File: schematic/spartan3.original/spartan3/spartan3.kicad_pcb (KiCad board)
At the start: 2 copper layers, 215.9 x 160 mm, 242 parts, among them U1_clk_select_0 SPFT_Sliding_Switch-dynacore, U2 XC3S250E-4TQG144C

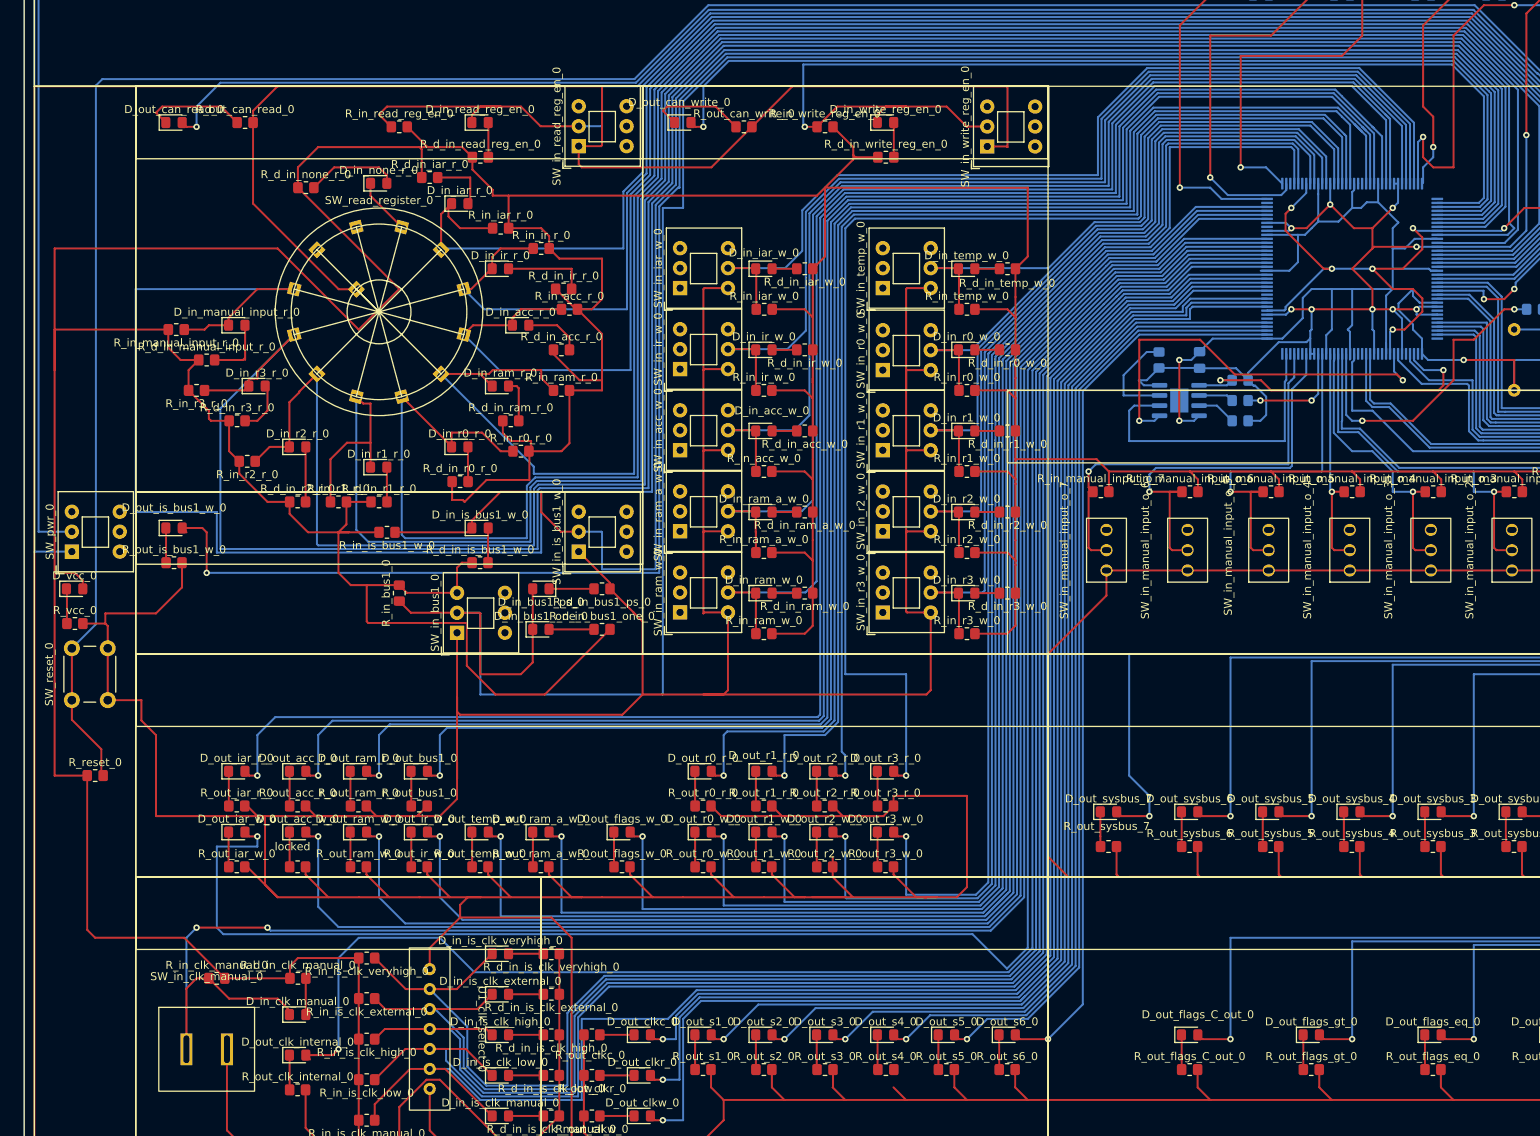
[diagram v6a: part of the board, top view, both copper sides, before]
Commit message: Tactile switch footprint updated. DRC rules checked/fixed
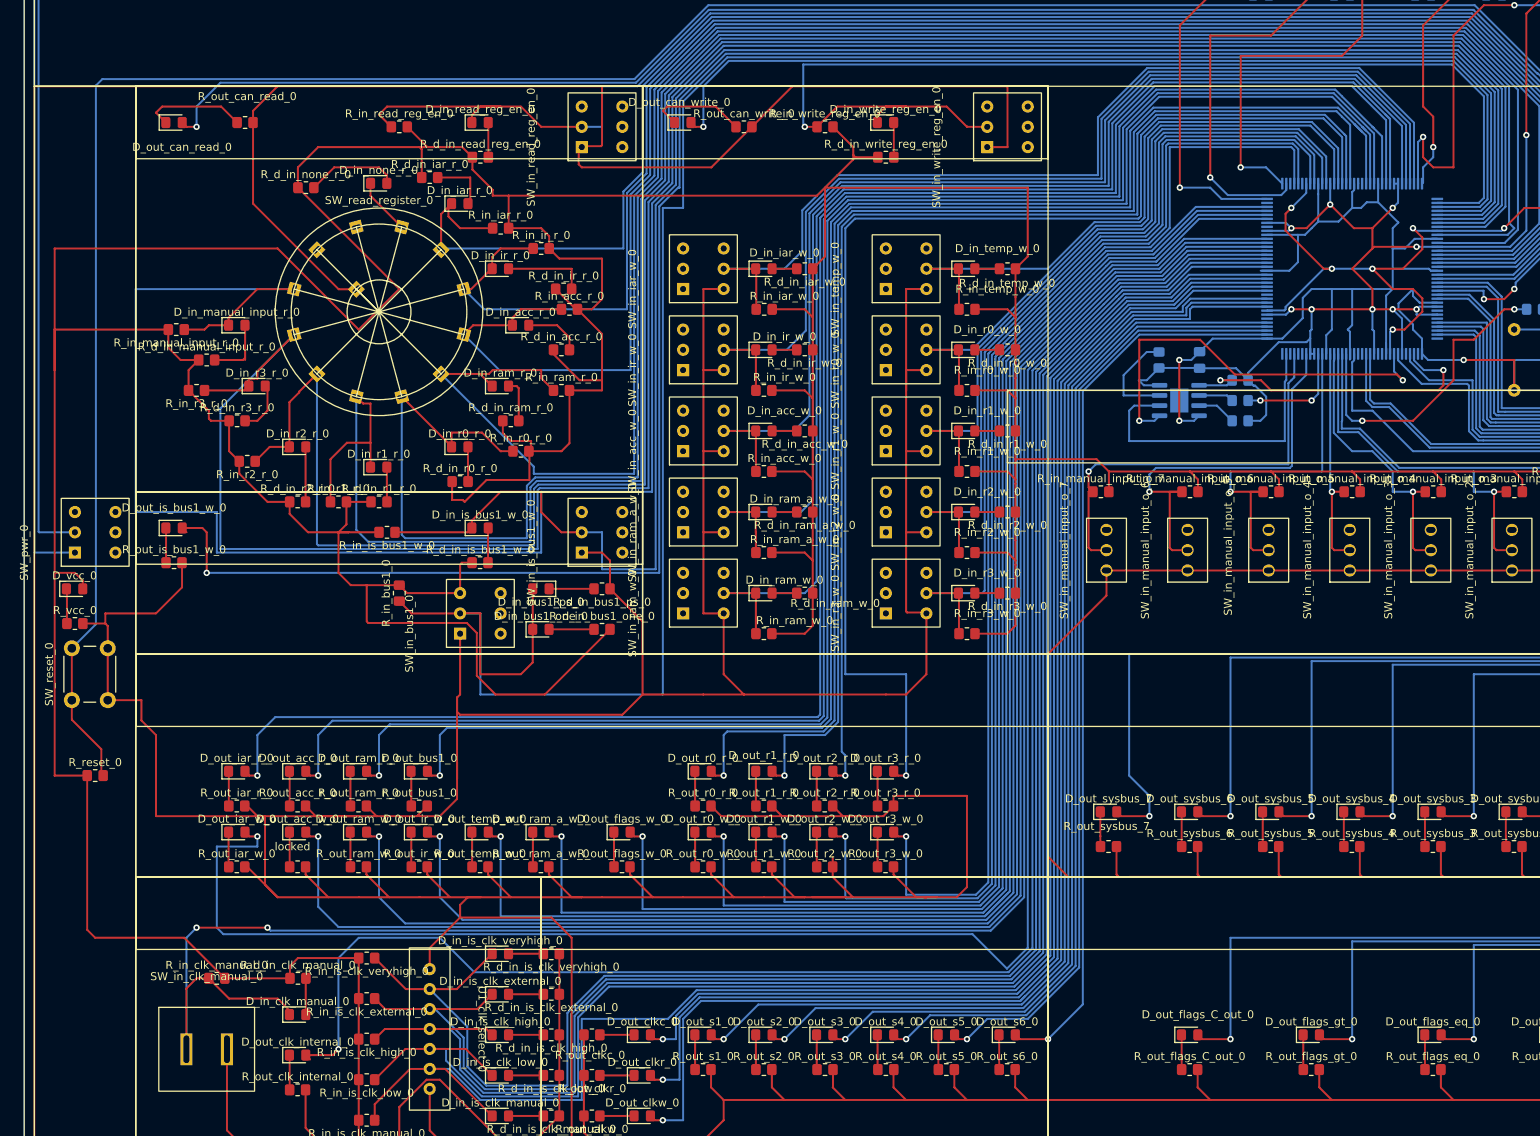
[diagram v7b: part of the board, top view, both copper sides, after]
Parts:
- SW_in_acc_w_0, SW_in_bus1_0, SW_in_iar_w_0, SW_in_ir_w_0, SW_in_is_bus1_w_0, SW_in_r0_w_0, SW_in_r1_w_0, SW_in_r2_w_0, SW_in_r3_w_0, SW_in_ram_a_w_0, SW_in_ram_w_0, SW_in_read_reg_en_0, SW_in_temp_w_0, SW_in_write_reg_en_0, SW_pwr_0: footprint Button_Switch_THT:SW_Push_2P2T_Toggle_CK_PVA2OAH5xxxxxxV2 -> SW_SPDT_small:Tactile_6PIN_SPDT_8.5x8.5mm
- moved SW_in_acc_w_0 0.40 mm to (81.3, 71.1)
- moved SW_in_ir_w_0 0.40 mm to (81.3, 61.0)
- moved SW_in_ram_a_w_0 0.40 mm to (81.3, 81.3)
- moved SW_in_ram_w_0 0.40 mm to (81.3, 91.4)
- moved SW_in_r1_w_0 0.40 mm to (106.7, 71.1)
- moved SW_in_r2_w_0 0.40 mm to (106.7, 81.3)
- moved SW_in_iar_w_0 0.40 mm to (81.3, 50.8)
- moved SW_in_temp_w_0 0.40 mm to (106.7, 50.8)
- moved SW_in_r3_w_0 0.40 mm to (106.7, 91.4)
- moved SW_in_bus1_0 0.40 mm to (53.3, 94.0)
- moved SW_pwr_0 0.40 mm to (5.08, 83.8)
- moved SW_in_read_reg_en_0 0.40 mm to (68.6, 33.0)
- moved SW_in_is_bus1_w_0 0.40 mm to (68.6, 83.8)
- moved SW_in_r0_w_0 0.38 mm to (106.7, 61.0)
- moved SW_in_write_reg_en_0 0.08 mm to (119.4, 33.0)
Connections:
- net gnd renamed GND
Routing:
- net GND: track 1881.4 -> 1876.0 mm
- net P140: track 141.3 -> 142.5 mm
- net P139: track 150.8 -> 152.0 mm
- net P141: track 131.8 -> 133.0 mm
- net P136: track 160.5 -> 161.8 mm
- net P142: track 122.6 -> 123.9 mm
- net P120: track 90.4 -> 91.6 mm
- net P117: track 108.3 -> 109.5 mm
- net P123: track 79.0 -> 80.2 mm
- net P119: track 99.7 -> 100.8 mm
- net P122: track 82.3 -> 83.3 mm

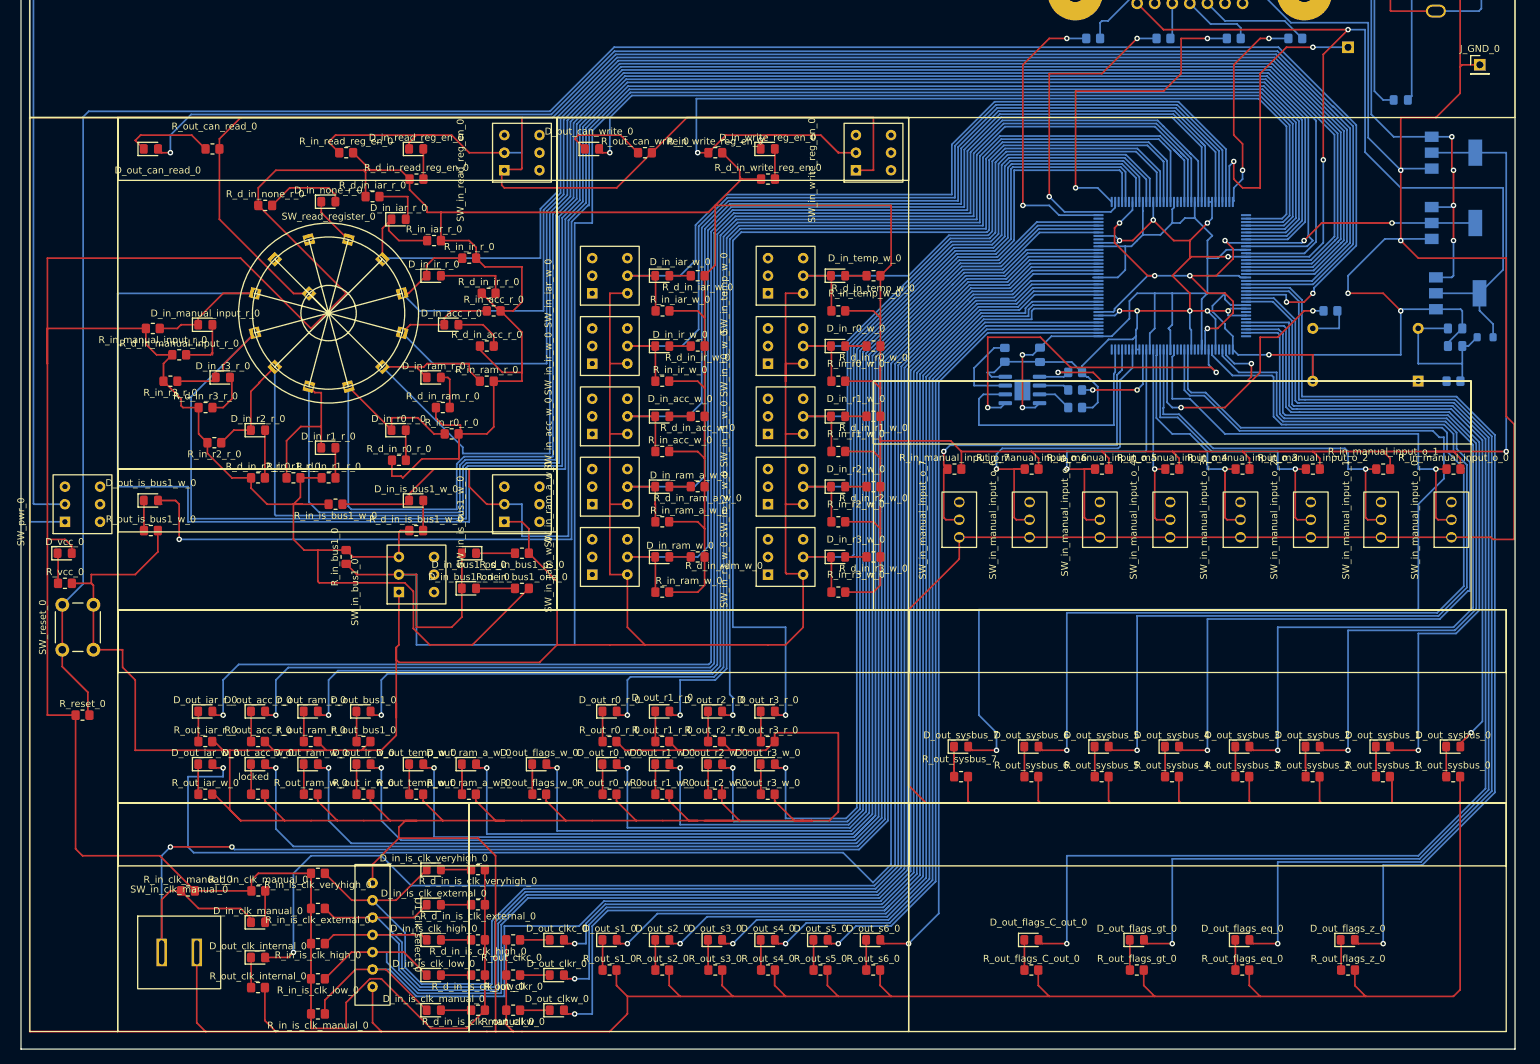
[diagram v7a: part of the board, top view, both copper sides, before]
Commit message: Schematics :: power capicators added. PCB layout :: labels updated
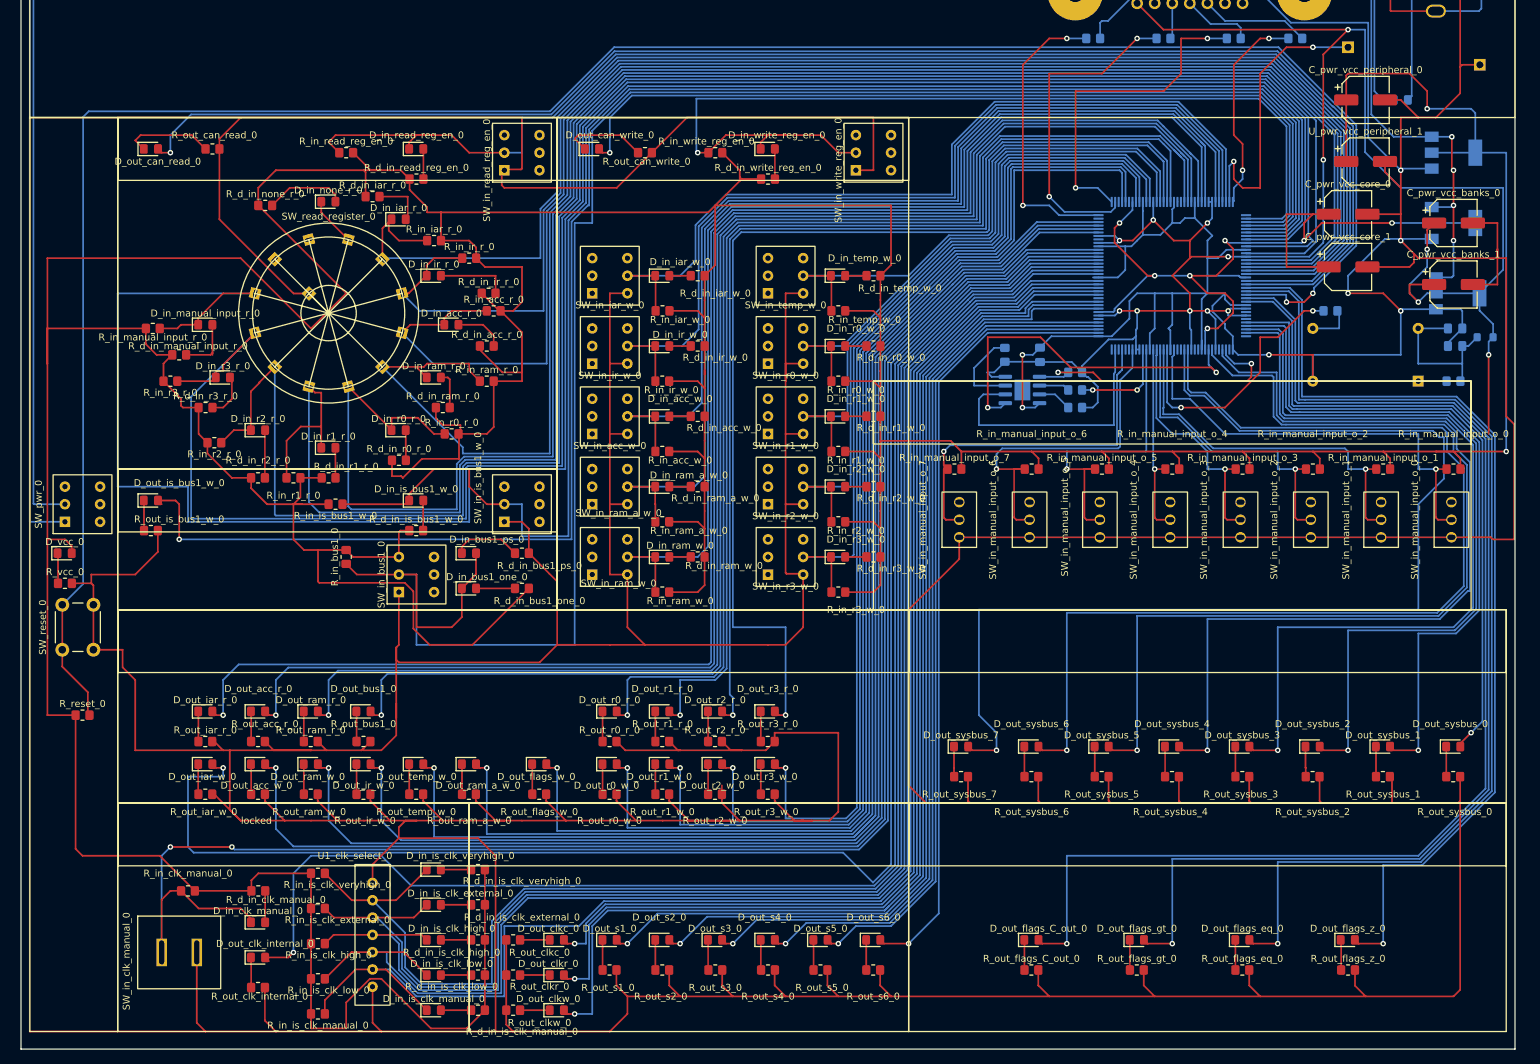
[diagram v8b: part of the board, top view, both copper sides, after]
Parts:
- added C_pwr_vcc_banks_0: 100uF, Capacitor_SMD:CP_Elec_6.3x5.4, F.Cu at (205.7, 40.6)
- added C_pwr_vcc_banks_1: 100uF, Capacitor_SMD:CP_Elec_6.3x5.4, F.Cu at (205.7, 49.5)
- added C_pwr_vcc_core_0: 100uF, Capacitor_SMD:CP_Elec_6.3x5.4, F.Cu at (190.5, 39.4)
- added C_pwr_vcc_core_1: 100uF, Capacitor_SMD:CP_Elec_6.3x5.4, F.Cu at (190.5, 47.0)
- added C_pwr_vcc_peripheral_0: 100uF, Capacitor_SMD:CP_Elec_6.3x5.4, F.Cu at (193.0, 22.9)
- added U_pwr_vcc_peripheral_1: 100uF, Capacitor_SMD:CP_Elec_6.3x5.4, F.Cu at (193.0, 31.8)
- J_GND_0: moved to B.Cu
- turned D_in_bus1_ps_0 to 0 degrees
- turned J_GND_0 to 180 degrees
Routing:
- net GND: track 1876.0 -> 1916.9 mm
- net VCC: track 974.8 -> 1015.6 mm, vias 1 -> 2
- net VCC_banks: track 277.5 -> 314.9 mm, vias 11 -> 14
- net VCC_core: track 95.5 -> 119.6 mm
- net Net-(D_in_bus1_ps_0-Pad1): track 5.64 -> 9.89 mm
- net P4: track 273.3 -> 274.2 mm
